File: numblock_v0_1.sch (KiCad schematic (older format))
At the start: 53 parts, among them J1 Conn_01x14_Female, J2 Conn_01x14_Female, J3 Conn_01x05_Female, SW1 SW_PUSH-MX_W_LED, SW10 SW_PUSH-MX_W_LED, SW11 SW_PUSH-MX_W_LED, SW12 SW_PUSH-MX_W_LED, SW13 SW_PUSH-MX_W_LED, SW14 SW_PUSH-MX_W_LED, SW15 SW_PUSH-MX_W_LED, SW16 SW_PUSH-MX_W_LED, SW17 SW_PUSH-MX_W_LED, SW18 SW_PUSH-MX_W_LED, SW19 SW_PUSH-MX_W_LED, SW2 SW_PUSH-MX_W_LED, SW20 SW_PUSH-MX_W_LED, SW21 Rotary_Encoder_Switch, SW22 Rotary_Encoder_Switch, SW3 SW_PUSH-MX_W_LED, SW4 SW_PUSH-MX_W_LED, SW5 SW_PUSH-MX_W_LED, SW6 SW_PUSH-MX_W_LED, SW7 SW_PUSH-MX_W_LED, SW8 SW_PUSH-MX_W_LED, SW9 SW_PUSH-MX_W_LED

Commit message: done for tonight
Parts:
- added H10, H11, H12, H13, H14, H15, H9: MountingHole_Pad, sofle RGB:hole_30mil, symbol Mechanical:MountingHole_Pad
- SW22: footprint sofle RGB:RotaryEncoder_Alps_EC11E-Switch_Vertical_H20mm_NoMountingHoles -> Rotary_Encoder:RotaryEncoder_Alps_EC11E-Switch_Vertical_H20mm_CircularMountingHoles
- gave numbers to parts that had none: 2
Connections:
- net GND: now also SW22.S1; no longer SW22.S2
- net Rot1: now also J2.7 (Pin_7), H9.1; no longer J2.8 (Pin_8), SW22.A
- net Rot2: now also J2.6 (Pin_6), H13.1; no longer J2.7 (Pin_7), SW22.B
- net SW: now also H12.1; no longer SW22.S1
- new net: H10.1, SW22.A
- new net: H14.1, SW22.B
- new net: H11.1, SW22.S2
- new net A2: H15.1, J2.8 (Pin_8)
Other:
- moved on the sheet: SW22
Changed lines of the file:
@@
 Wire Wire Line
 	4650 1450 4850 1450
-Text Label 4850 1450 0    50   ~ 0
-SW
 Wire Wire Line
 	1350 1600 1050 1600
 Text Label 1050 1600 0    50   ~ 0
 SW
-Text Label 3850 1450 0    50   ~ 0
+Wire Wire Line
+	3850 1650 4050 1650
+Wire Wire Line
+	4050 1450 3850 1450
+Text Label 2550 2000 2    50   ~ 0
 Rot1
-Text Label 3850 1650 0    50   ~ 0
+Text Label 2550 2100 2    50   ~ 0
 Rot2
 Wire Wire Line
-	3850 1650 4050 1650
-Wire Wire Line
-	4050 1450 3850 1450
-Text Label 2550 1900 2    50   ~ 0
-Rot1
-Text Label 2550 2000 2    50   ~ 0
-Rot2
-Wire Wire Line
-	2550 2000 2350 2000
-Wire Wire Line
-	2350 1900 2550 1900
+	2550 2100 2350 2100
+Wire Wire Line
+	2350 2000 2550 2000
 Text Label 1050 2600 0    50   ~ 0
 RX
@@
 L Device:Rotary_Encoder_Switch SW22
 U 1 1 609EC679
-P 5900 1550
-F 0 "SW22" H 5900 1917 50  0000 C CNN
-F 1 "Rotary_Encoder_Switch" H 5900 1826 50  0000 C CNN
-F 2 "sofle RGB:RotaryEncoder_Alps_EC11E-Switch_Vertical_H20mm_NoMountingHoles" H 5750 1710 50  0001 C CNN
-F 3 "~" H 5900 1810 50  0001 C CNN
-	1    5900 1550
+P 7100 1650
+F 0 "SW22" H 7100 2017 50  0000 C CNN
+F 1 "Rotary_Encoder_Switch" H 7100 1926 50  0000 C CNN
+F 2 "Rotary_Encoder:RotaryEncoder_Alps_EC11E-Switch_Vertical_H20mm_CircularMountingHoles" H 6950 1810 50  0001 C CNN
+F 3 "~" H 7100 1910 50  0001 C CNN
+	1    7100 1650
 	1    0    0    -1
 $EndComp
 Wire Wire Line
-	6200 1450 6400 1450
-Text Label 6400 1450 0    50   ~ 0
-SW
-Text Label 5400 1450 0    50   ~ 0
-Rot1
-Text Label 5400 1650 0    50   ~ 0
-Rot2
-Wire Wire Line
-	5400 1650 5600 1650
-Wire Wire Line
-	5600 1450 5400 1450
+	7900 1100 8100 1100
+Wire Wire Line
+	6050 1200 6250 1200
+Wire Wire Line
+	6250 1000 6050 1000
 $Comp
 L power:GND #PWR0105
 U 1 1 609ECC55
-P 6350 1650
-F 0 "#PWR0105" H 6350 1400 50  0001 C CNN
-F 1 "GND" V 6355 1522 50  0000 R CNN
-F 2 "" H 6350 1650 50  0001 C CNN
-F 3 "" H 6350 1650 50  0001 C CNN
-	1    6350 1650
+P 7550 1550
+F 0 "#PWR0105" H 7550 1300 50  0001 C CNN
+F 1 "GND" V 7555 1422 50  0000 R CNN
+F 2 "" H 7550 1550 50  0001 C CNN
+F 3 "" H 7550 1550 50  0001 C CNN
+	1    7550 1550
 	0    -1   -1   0
 $EndComp
 Wire Wire Line
-	6350 1650 6200 1650
-$Comp
-L power:GND #PWR0106
-U 1 1 609ECC60
-P 5500 1550
-F 0 "#PWR0106" H 5500 1300 50  0001 C CNN
-F 1 "GND" V 5505 1422 50  0000 R CNN
-F 2 "" H 5500 1550 50  0001 C CNN
-F 3 "" H 5500 1550 50  0001 C CNN
-	1    5500 1550
-	0    1    1    0
-$EndComp
-Wire Wire Line
-	5500 1550 5600 1550
+	7550 1550 7400 1550
+Wire Wire Line
+	1200 6600 900  6600
+Wire Wire Line
+	1200 6400 900  6400
+$Comp
+L Mechanical:MountingHole_Pad H7
+U 1 1 60A6EC20
+P 1300 6400
+F 0 "H7" V 1254 6550 50  0000 L CNN
+F 1 "MountingHole_Pad" V 1345 6550 50  0000 L CNN
+F 2 "sofle RGB:hole_30mil" H 1300 6400 50  0001 C CNN
+F 3 "~" H 1300 6400 50  0001 C CNN
+	1    1300 6400
+	0    1    1    0
+$EndComp
+$Comp
+L Mechanical:MountingHole_Pad H8
+U 1 1 60A6EC2A
+P 1300 6600
+F 0 "H8" V 1254 6750 50  0000 L CNN
+F 1 "MountingHole_Pad" V 1345 6750 50  0000 L CNN
+F 2 "sofle RGB:hole_30mil" H 1300 6600 50  0001 C CNN
+F 3 "~" H 1300 6600 50  0001 C CNN
+	1    1300 6600
+	0    1    1    0
+$EndComp
+Text Label 8100 1100 0    50   ~ 0
+SW
+Text Label 4850 1450 0    50   ~ 0
+SW
+Text Label 6050 1200 0    50   ~ 0
+Rot2
+Text Label 6050 1000 0    50   ~ 0
+Rot1
+Text Label 3850 1650 0    50   ~ 0
+Rot2
+Text Label 3850 1450 0    50   ~ 0
+Rot1
 Text Label 900  6400 0    50   ~ 0
 A0
@@
 A1
 Wire Wire Line
-	1200 6600 900  6600
-Wire Wire Line
-	1200 6400 900  6400
-$Comp
-L Mechanical:MountingHole_Pad H?
-U 1 1 60A6EC20
-P 1300 6400
-F 0 "H?" V 1254 6550 50  0000 L CNN
-F 1 "MountingHole_Pad" V 1345 6550 50  0000 L CNN
-F 2 "sofle RGB:hole_30mil" H 1300 6400 50  0001 C CNN
-F 3 "~" H 1300 6400 50  0001 C CNN
-	1    1300 6400
-	0    1    1    0
-$EndComp
-$Comp
-L Mechanical:MountingHole_Pad H?
-U 1 1 60A6EC2A
-P 1300 6600
-F 0 "H?" V 1254 6750 50  0000 L CNN
-F 1 "MountingHole_Pad" V 1345 6750 50  0000 L CNN
-F 2 "sofle RGB:hole_30mil" H 1300 6600 50  0001 C CNN
-F 3 "~" H 1300 6600 50  0001 C CNN
-	1    1300 6600
-	0    1    1    0
-$EndComp
+	2550 1800 2350 1800
+Wire Wire Line
+	2350 1700 2550 1700
 Text Label 2550 1700 2    50   ~ 0
 A0
 Text Label 2550 1800 2    50   ~ 0
 A1
-Wire Wire Line
-	2550 1800 2350 1800
-Wire Wire Line
-	2350 1700 2550 1700
+$Comp
+L Mechanical:MountingHole_Pad H9
+U 1 1 60B49CAD
+P 6350 1000
+F 0 "H9" V 6304 1150 50  0000 L CNN
+F 1 "MountingHole_Pad" V 6395 1150 50  0000 L CNN
+F 2 "sofle RGB:hole_30mil" H 6350 1000 50  0001 C CNN
+F 3 "~" H 6350 1000 50  0001 C CNN
+	1    6350 1000
+	0    1    1    0
+$EndComp
+$Comp
+L Mechanical:MountingHole_Pad H13
+U 1 1 60B4A2C5
+P 6350 1200
+F 0 "H13" V 6304 1350 50  0000 L CNN
+F 1 "MountingHole_Pad" V 6395 1350 50  0000 L CNN
+F 2 "sofle RGB:hole_30mil" H 6350 1200 50  0001 C CNN
+F 3 "~" H 6350 1200 50  0001 C CNN
+	1    6350 1200
+	0    1    1    0
+$EndComp
+$Comp
+L Mechanical:MountingHole_Pad H10
+U 1 1 60B4A2CF
+P 6700 1550
+F 0 "H10" V 6654 1700 50  0000 L CNN
+F 1 "MountingHole_Pad" V 6745 1700 50  0000 L CNN
+F 2 "sofle RGB:hole_30mil" H 6700 1550 50  0001 C CNN
+F 3 "~" H 6700 1550 50  0001 C CNN
+	1    6700 1550
+	0    -1   -1   0
+$EndComp
+$Comp
+L Mechanical:MountingHole_Pad H12
+U 1 1 60B4A2D9
+P 7800 1100
+F 0 "H12" V 7754 1250 50  0000 L CNN
+F 1 "MountingHole_Pad" V 7845 1250 50  0000 L CNN
+F 2 "sofle RGB:hole_30mil" H 7800 1100 50  0001 C CNN
+F 3 "~" H 7800 1100 50  0001 C CNN
+	1    7800 1100
+	0    -1   -1   0
+$EndComp
+$Comp
+L power:GND #PWR0106
+U 1 1 60B65776
+P 6500 1650
+F 0 "#PWR0106" H 6500 1400 50  0001 C CNN
+F 1 "GND" V 6505 1522 50  0000 R CNN
+F 2 "" H 6500 1650 50  0001 C CNN
+F 3 "" H 6500 1650 50  0001 C CNN
+	1    6500 1650
+	0    1    1    0
+$EndComp
+$Comp
+L Mechanical:MountingHole_Pad H11
+U 1 1 60B6D9A7
+P 7500 1750
+F 0 "H11" V 7454 1900 50  0000 L CNN
+F 1 "MountingHole_Pad" V 7545 1900 50  0000 L CNN
+F 2 "sofle RGB:hole_30mil" H 7500 1750 50  0001 C CNN
+F 3 "~" H 7500 1750 50  0001 C CNN
+	1    7500 1750
+	0    1    1    0
+$EndComp
+$Comp
+L Mechanical:MountingHole_Pad H14
+U 1 1 60B7E845
+P 6700 1750
+F 0 "H14" V 6654 1900 50  0000 L CNN
+F 1 "MountingHole_Pad" V 6745 1900 50  0000 L CNN
+F 2 "sofle RGB:hole_30mil" H 6700 1750 50  0001 C CNN
+F 3 "~" H 6700 1750 50  0001 C CNN
+	1    6700 1750
+	0    -1   -1   0
+$EndComp
+Wire Wire Line
+	6500 1650 6800 1650
+Wire Wire Line
+	2550 1900 2350 1900
+Text Label 2550 1900 2    50   ~ 0
+A2
+Wire Wire Line
+	1200 6800 900  6800
+$Comp
+L Mechanical:MountingHole_Pad H15
+U 1 1 60C0B11C
+P 1300 6800
+F 0 "H15" V 1254 6950 50  0000 L CNN
+F 1 "MountingHole_Pad" V 1345 6950 50  0000 L CNN
+F 2 "sofle RGB:hole_30mil" H 1300 6800 50  0001 C CNN
+F 3 "~" H 1300 6800 50  0001 C CNN
+	1    1300 6800
+	0    1    1    0
+$EndComp
+Text Label 900  6800 0    50   ~ 0
+A2
 $EndSCHEMATC

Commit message: about to add underglow
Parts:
- D1, D10, D11, D12, D13, D14, D15, D16, D17, D18, D19, D2, D20, D3, D4, D5, D6, D7, D8, D9: footprint Diode_SMD:D_0805_2012Metric_Pad1.15x1.40mm_HandSolder -> Diode_SMD:D_SOD-123
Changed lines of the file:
@@
 F 0 "D2" V 5154 3330 50  0000 L CNN
 F 1 "D" V 5245 3330 50  0000 L CNN
-F 2 "Diode_SMD:D_0805_2012Metric_Pad1.15x1.40mm_HandSolder" H 5200 3250 50  0001 C CNN
+F 2 "Diode_SMD:D_SOD-123" H 5200 3250 50  0001 C CNN
 F 3 "~" H 5200 3250 50  0001 C CNN
 	1    5200 3250
@@
 F 0 "D1" V 4154 3330 50  0000 L CNN
 F 1 "D" V 4245 3330 50  0000 L CNN
-F 2 "Diode_SMD:D_0805_2012Metric_Pad1.15x1.40mm_HandSolder" H 4200 3250 50  0001 C CNN
+F 2 "Diode_SMD:D_SOD-123" H 4200 3250 50  0001 C CNN
 F 3 "~" H 4200 3250 50  0001 C CNN
 	1    4200 3250
@@
 F 0 "D3" V 6154 3330 50  0000 L CNN
 F 1 "D" V 6245 3330 50  0000 L CNN
-F 2 "Diode_SMD:D_0805_2012Metric_Pad1.15x1.40mm_HandSolder" H 6200 3250 50  0001 C CNN
+F 2 "Diode_SMD:D_SOD-123" H 6200 3250 50  0001 C CNN
 F 3 "~" H 6200 3250 50  0001 C CNN
 	1    6200 3250
@@
 F 0 "D4" V 7154 3330 50  0000 L CNN
 F 1 "D" V 7245 3330 50  0000 L CNN
-F 2 "Diode_SMD:D_0805_2012Metric_Pad1.15x1.40mm_HandSolder" H 7200 3250 50  0001 C CNN
+F 2 "Diode_SMD:D_SOD-123" H 7200 3250 50  0001 C CNN
 F 3 "~" H 7200 3250 50  0001 C CNN
 	1    7200 3250
@@
 F 0 "D7" V 5154 4080 50  0000 L CNN
 F 1 "D" V 5245 4080 50  0000 L CNN
-F 2 "Diode_SMD:D_0805_2012Metric_Pad1.15x1.40mm_HandSolder" H 5200 4000 50  0001 C CNN
+F 2 "Diode_SMD:D_SOD-123" H 5200 4000 50  0001 C CNN
 F 3 "~" H 5200 4000 50  0001 C CNN
 	1    5200 4000
@@
 F 0 "D8" V 6154 4080 50  0000 L CNN
 F 1 "D" V 6245 4080 50  0000 L CNN
-F 2 "Diode_SMD:D_0805_2012Metric_Pad1.15x1.40mm_HandSolder" H 6200 4000 50  0001 C CNN
+F 2 "Diode_SMD:D_SOD-123" H 6200 4000 50  0001 C CNN
 F 3 "~" H 6200 4000 50  0001 C CNN
 	1    6200 4000
@@
 F 0 "D9" V 7154 4080 50  0000 L CNN
 F 1 "D" V 7245 4080 50  0000 L CNN
-F 2 "Diode_SMD:D_0805_2012Metric_Pad1.15x1.40mm_HandSolder" H 7200 4000 50  0001 C CNN
+F 2 "Diode_SMD:D_SOD-123" H 7200 4000 50  0001 C CNN
 F 3 "~" H 7200 4000 50  0001 C CNN
 	1    7200 4000
@@
 F 0 "D6" V 4154 4080 50  0000 L CNN
 F 1 "D" V 4245 4080 50  0000 L CNN
-F 2 "Diode_SMD:D_0805_2012Metric_Pad1.15x1.40mm_HandSolder" H 4200 4000 50  0001 C CNN
+F 2 "Diode_SMD:D_SOD-123" H 4200 4000 50  0001 C CNN
 F 3 "~" H 4200 4000 50  0001 C CNN
 	1    4200 4000
@@
 F 0 "D12" V 5154 4830 50  0000 L CNN
 F 1 "D" V 5245 4830 50  0000 L CNN
-F 2 "Diode_SMD:D_0805_2012Metric_Pad1.15x1.40mm_HandSolder" H 5200 4750 50  0001 C CNN
+F 2 "Diode_SMD:D_SOD-123" H 5200 4750 50  0001 C CNN
 F 3 "~" H 5200 4750 50  0001 C CNN
 	1    5200 4750
@@
 F 0 "D13" V 6154 4830 50  0000 L CNN
 F 1 "D" V 6245 4830 50  0000 L CNN
-F 2 "Diode_SMD:D_0805_2012Metric_Pad1.15x1.40mm_HandSolder" H 6200 4750 50  0001 C CNN
+F 2 "Diode_SMD:D_SOD-123" H 6200 4750 50  0001 C CNN
 F 3 "~" H 6200 4750 50  0001 C CNN
 	1    6200 4750
@@
 F 0 "D14" V 7154 4830 50  0000 L CNN
 F 1 "D" V 7245 4830 50  0000 L CNN
-F 2 "Diode_SMD:D_0805_2012Metric_Pad1.15x1.40mm_HandSolder" H 7200 4750 50  0001 C CNN
+F 2 "Diode_SMD:D_SOD-123" H 7200 4750 50  0001 C CNN
 F 3 "~" H 7200 4750 50  0001 C CNN
 	1    7200 4750
@@
 F 0 "D11" V 4154 4830 50  0000 L CNN
 F 1 "D" V 4245 4830 50  0000 L CNN
-F 2 "Diode_SMD:D_0805_2012Metric_Pad1.15x1.40mm_HandSolder" H 4200 4750 50  0001 C CNN
+F 2 "Diode_SMD:D_SOD-123" H 4200 4750 50  0001 C CNN
 F 3 "~" H 4200 4750 50  0001 C CNN
 	1    4200 4750
@@
 F 0 "D17" V 5154 5580 50  0000 L CNN
 F 1 "D" V 5245 5580 50  0000 L CNN
-F 2 "Diode_SMD:D_0805_2012Metric_Pad1.15x1.40mm_HandSolder" H 5200 5500 50  0001 C CNN
+F 2 "Diode_SMD:D_SOD-123" H 5200 5500 50  0001 C CNN
 F 3 "~" H 5200 5500 50  0001 C CNN
 	1    5200 5500
@@
 F 0 "D18" V 6154 5580 50  0000 L CNN
 F 1 "D" V 6245 5580 50  0000 L CNN
-F 2 "Diode_SMD:D_0805_2012Metric_Pad1.15x1.40mm_HandSolder" H 6200 5500 50  0001 C CNN
+F 2 "Diode_SMD:D_SOD-123" H 6200 5500 50  0001 C CNN
 F 3 "~" H 6200 5500 50  0001 C CNN
 	1    6200 5500
@@
 F 0 "D19" V 7154 5580 50  0000 L CNN
 F 1 "D" V 7245 5580 50  0000 L CNN
-F 2 "Diode_SMD:D_0805_2012Metric_Pad1.15x1.40mm_HandSolder" H 7200 5500 50  0001 C CNN
+F 2 "Diode_SMD:D_SOD-123" H 7200 5500 50  0001 C CNN
 F 3 "~" H 7200 5500 50  0001 C CNN
 	1    7200 5500
@@
 F 0 "D16" V 4154 5580 50  0000 L CNN
 F 1 "D" V 4245 5580 50  0000 L CNN
-F 2 "Diode_SMD:D_0805_2012Metric_Pad1.15x1.40mm_HandSolder" H 4200 5500 50  0001 C CNN
+F 2 "Diode_SMD:D_SOD-123" H 4200 5500 50  0001 C CNN
 F 3 "~" H 4200 5500 50  0001 C CNN
 	1    4200 5500
@@
 F 0 "D5" V 8154 3330 50  0000 L CNN
 F 1 "D" V 8245 3330 50  0000 L CNN
-F 2 "Diode_SMD:D_0805_2012Metric_Pad1.15x1.40mm_HandSolder" H 8200 3250 50  0001 C CNN
+F 2 "Diode_SMD:D_SOD-123" H 8200 3250 50  0001 C CNN
 F 3 "~" H 8200 3250 50  0001 C CNN
 	1    8200 3250
@@
 F 0 "D10" V 8154 4080 50  0000 L CNN
 F 1 "D" V 8245 4080 50  0000 L CNN
-F 2 "Diode_SMD:D_0805_2012Metric_Pad1.15x1.40mm_HandSolder" H 8200 4000 50  0001 C CNN
+F 2 "Diode_SMD:D_SOD-123" H 8200 4000 50  0001 C CNN
 F 3 "~" H 8200 4000 50  0001 C CNN
 	1    8200 4000
@@
 F 0 "D15" V 8154 4830 50  0000 L CNN
 F 1 "D" V 8245 4830 50  0000 L CNN
-F 2 "Diode_SMD:D_0805_2012Metric_Pad1.15x1.40mm_HandSolder" H 8200 4750 50  0001 C CNN
+F 2 "Diode_SMD:D_SOD-123" H 8200 4750 50  0001 C CNN
 F 3 "~" H 8200 4750 50  0001 C CNN
 	1    8200 4750
@@
 F 0 "D20" V 8154 5580 50  0000 L CNN
 F 1 "D" V 8245 5580 50  0000 L CNN
-F 2 "Diode_SMD:D_0805_2012Metric_Pad1.15x1.40mm_HandSolder" H 8200 5500 50  0001 C CNN
+F 2 "Diode_SMD:D_SOD-123" H 8200 5500 50  0001 C CNN
 F 3 "~" H 8200 5500 50  0001 C CNN
 	1    8200 5500

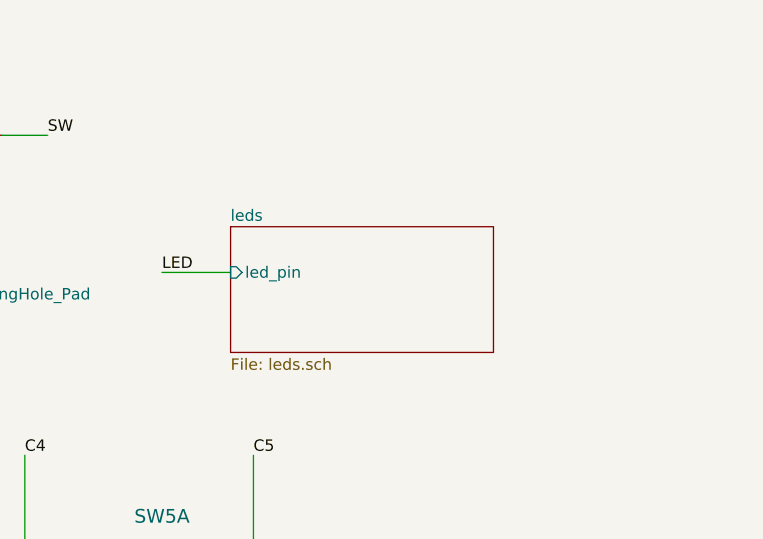
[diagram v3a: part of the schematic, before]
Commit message: added top led and oled display support
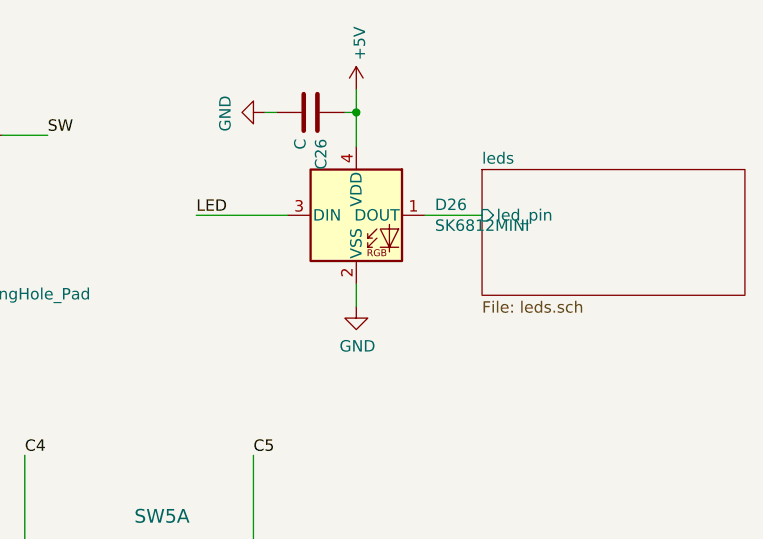
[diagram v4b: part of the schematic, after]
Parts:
- added C26: C, Capacitor_SMD:C_0805_2012Metric_Pad1.18x1.45mm_HandSolder, symbol Device:C
- added D26: SK6812MINI, LED_SMD:LED_SK6812MINI_PLCC4_3.5x3.5mm_P1.75mm, symbol LED:SK6812MINI
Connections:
- net +5V: now also C26.1, D26.4 (VDD)
- net GND: now also C26.2, D26.2 (VSS)
- net LED: now also D26.3 (DIN)
- new net leds/led_pin: D26.1 (DOUT)
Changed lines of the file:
@@
 $EndComp
 $Sheet
-S 8900 1500 1150 550
+S 10000 1250 1150 550
 U 60AEFC05
 F0 "leds" 50
 F1 "leds.sch" 50
-F2 "led_pin" I L 8900 1700 50
+F2 "led_pin" I L 10000 1450 50
 $EndSheet
-Text Label 8600 1700 0    50   ~ 0
+Text Label 8750 1450 0    50   ~ 0
 LED
-Wire Wire Line
-	8600 1700 8900 1700
 $Comp
 L sofle_rgb:SW_PUSH-MX_W_LED SW5
@@
 Text Label 900  6800 0    50   ~ 0
 A2
+$Comp
+L LED:SK6812MINI D26
+U 1 1 60A321EC
+P 9450 1450
+F 0 "D26" H 9794 1496 50  0000 L CNN
+F 1 "SK6812MINI" H 9794 1405 50  0000 L CNN
+F 2 "LED_SMD:LED_SK6812MINI_PLCC4_3.5x3.5mm_P1.75mm" H 9500 1150 50  0001 L TNN
+F 3 "https://cdn-shop.adafruit.com/product-files/2686/SK6812MINI_REV.01-1-2.pdf" H 9550 1075 50  0001 L TNN
+	1    9450 1450
+	1    0    0    -1
+$EndComp
+$Comp
+L power:+5V #PWR?
+U 1 1 60A4B915
+P 9450 900
+AR Path="/60AEFC05/60A4B915" Ref="#PWR?"  Part="1"
+AR Path="/60A4B915" Ref="#PWR0122"  Part="1"
+F 0 "#PWR0122" H 9450 750 50  0001 C CNN
+F 1 "+5V" V 9465 1028 50  0000 L CNN
+F 2 "" H 9450 900 50  0001 C CNN
+F 3 "" H 9450 900 50  0001 C CNN
+	1    9450 900
+	1    0    0    -1
+$EndComp
+$Comp
+L power:GND #PWR?
+U 1 1 60A4B91B
+P 9050 1000
+AR Path="/60AEFC05/60A4B91B" Ref="#PWR?"  Part="1"
+AR Path="/60A4B91B" Ref="#PWR0123"  Part="1"
+F 0 "#PWR0123" H 9050 750 50  0001 C CNN
+F 1 "GND" H 9055 827 50  0000 C CNN
+F 2 "" H 9050 1000 50  0001 C CNN
+F 3 "" H 9050 1000 50  0001 C CNN
+	1    9050 1000
+	0    1    1    0
+$EndComp
+Wire Wire Line
+	9050 1000 9100 1000
+Wire Wire Line
+	9400 1000 9450 1000
+Wire Wire Line
+	9450 1000 9450 900
+Wire Wire Line
+	9450 1150 9450 1000
+Connection ~ 9450 1000
+$Comp
+L Device:C C?
+U 1 1 60A4B926
+P 9250 1000
+AR Path="/60AEFC05/60A4B926" Ref="C?"  Part="1"
+AR Path="/60A4B926" Ref="C26"  Part="1"
+F 0 "C26" H 9365 1046 50  0000 L CNN
+F 1 "C" H 9365 955 50  0000 L CNN
+F 2 "Capacitor_SMD:C_0805_2012Metric_Pad1.18x1.45mm_HandSolder" H 9288 850 50  0001 C CNN
+F 3 "~" H 9250 1000 50  0001 C CNN
+	1    9250 1000
+	0    1    1    0
+$EndComp
+$Comp
+L power:GND #PWR0124
+U 1 1 60A5FD08
+P 9450 1850
+F 0 "#PWR0124" H 9450 1600 50  0001 C CNN
+F 1 "GND" H 9455 1677 50  0000 C CNN
+F 2 "" H 9450 1850 50  0001 C CNN
+F 3 "" H 9450 1850 50  0001 C CNN
+	1    9450 1850
+	1    0    0    -1
+$EndComp
+Wire Wire Line
+	9450 1850 9450 1750
+Wire Wire Line
+	8750 1450 9150 1450
+Wire Wire Line
+	9750 1450 10000 1450
 $EndSCHEMATC

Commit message: fixed backlight leds; added holes
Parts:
- D26: footprint LED_SMD:LED_SK6812MINI_PLCC4_3.5x3.5mm_P1.75mm -> sofle RGB:LED_SK6812MINI_HS
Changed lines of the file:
@@
 F 0 "D26" H 9794 1496 50  0000 L CNN
 F 1 "SK6812MINI" H 9794 1405 50  0000 L CNN
-F 2 "LED_SMD:LED_SK6812MINI_PLCC4_3.5x3.5mm_P1.75mm" H 9500 1150 50  0001 L TNN
+F 2 "sofle RGB:LED_SK6812MINI_HS" H 9500 1150 50  0001 L TNN
 F 3 "https://cdn-shop.adafruit.com/product-files/2686/SK6812MINI_REV.01-1-2.pdf" H 9550 1075 50  0001 L TNN
 	1    9450 1450

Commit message: replaced plated mountig holes to unplated; final touches before placing order
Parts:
- SW22: footprint Rotary_Encoder:RotaryEncoder_Alps_EC11E-Switch_Vertical_H20mm_CircularMountingHoles -> sofle RGB:RotaryEncoder_Alps_EC11E-Switch_Vertical_H20mm-keebio_modified
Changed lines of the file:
@@
 F 0 "SW22" H 7100 2017 50  0000 C CNN
 F 1 "Rotary_Encoder_Switch" H 7100 1926 50  0000 C CNN
-F 2 "Rotary_Encoder:RotaryEncoder_Alps_EC11E-Switch_Vertical_H20mm_CircularMountingHoles" H 6950 1810 50  0001 C CNN
+F 2 "sofle RGB:RotaryEncoder_Alps_EC11E-Switch_Vertical_H20mm-keebio_modified" H 6950 1810 50  0001 C CNN
 F 3 "~" H 7100 1910 50  0001 C CNN
 	1    7100 1650
